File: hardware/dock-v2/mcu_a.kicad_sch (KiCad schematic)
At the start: 29 parts, among them SW301 SW_Push, SW302 SW_Push, U301 RP2354A, Y301 12MHz

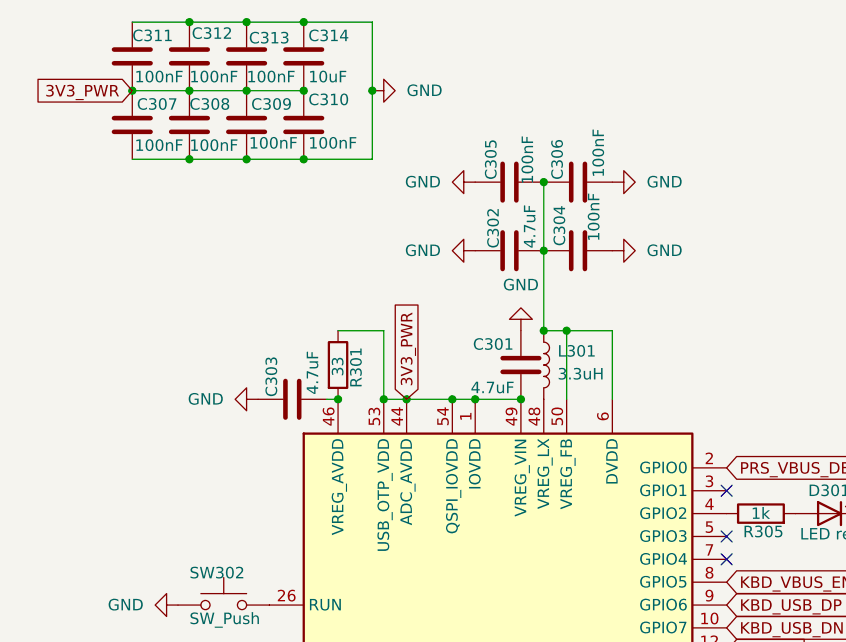
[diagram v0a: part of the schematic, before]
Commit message: Dock v2 schematic: PWR_FLAGs, one name per power net, ESP32 USB test pads dropped
- PWR_FLAGs on GND, VBUS_IN, 5V_PWR, A_1V1, A_VREG_AVDD, B_1V1, B_VREG_AVDD
  (each with a label at a pin of the net, which also names the five nets that
  were unnamed: VBUS_IN, A/B_1V1, A/B_VREG_AVDD)
- GNDPWR symbol -> GND; duplicate +3.3V/+5V power symbols and their now-dangling
  3V3_PWR/5V_PWR labels removed (connectivity verified identical before/after)
- TP501/TP502 (ESP32 GPIO18/19 USB pads) not needed: pins 26/27 are no-connects
  in the model; docs and guides updated (fallback flashing: TXD0/RXD0 pads)

ERC: 0 errors, 0 warnings. check_wiring.py: OK, wiring matches the guide.

Co-Authored-By: Claude Opus 5.5 <noreply@anthropic.com>
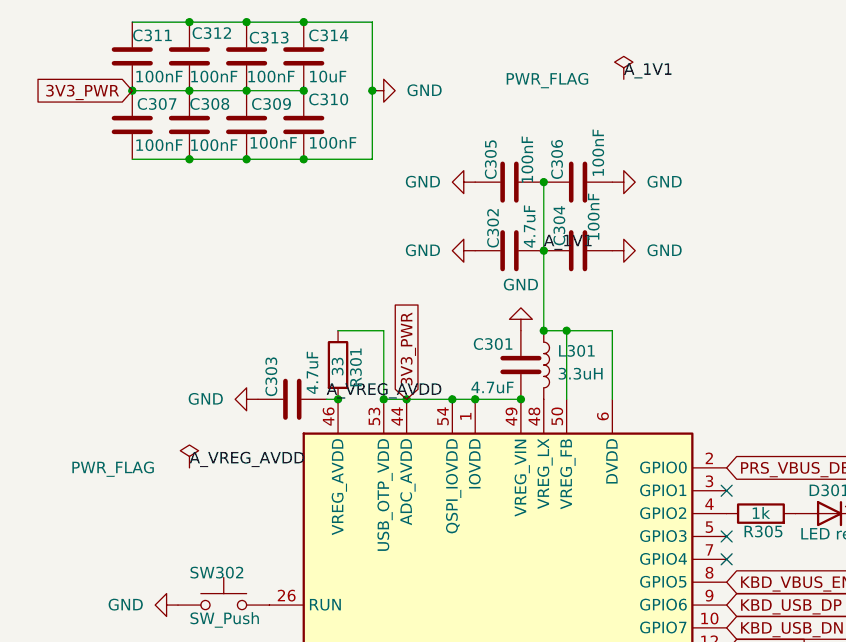
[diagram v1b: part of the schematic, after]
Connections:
- net A_1V1: now reaches C302.2, C304.1, C305.2, C306.1, L301.1, U301.23 (DVDD), U301.39 (DVDD), U301.50 (VREG_FB), U301.6 (DVDD)
- net A_VREG_AVDD: now reaches C303.2, R301.2, U301.46 (VREG_AVDD)
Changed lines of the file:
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@@
+		)
+	)
+	(label "A_1V1"
+		(at 189.23 57.15 0)
+		(fields_autoplaced yes)
+		(effects
+			(font
+				(size 1.27 1.27)
+			)
+			(justify left bottom)
+		)
+	)
+	(symbol
+		(lib_id "power:PWR_FLAG")
+		(at 198.12 38.1 0)
+		(unit 1)
+		(body_style 1)
+		(exclude_from_sim no)
+		(in_bom yes)
+		(on_board yes)
+		(in_pos_files yes)
+		(dnp no)
+		(fields_autoplaced yes)
+		(property "Reference" "#FLG0390"
+			(at 191.77 38.1 0)
+			(hide yes)
+			(show_name no)
+			(do_not_autoplace no)
+			(effects
+				(font
+					(size 1.27 1.27)
+				)
+			)
+		)
+		(property "Value" "PWR_FLAG"
+			(at 194.31 38.1 0)
+			(show_name no)
+			(do_not_autoplace no)
+			(effects
+				(font
+					(size 1.27 1.27)
+				)
+				(justify right)
+			)
+		)
+		(property "Footprint" ""
+			(at 198.12 38.1 0)
+			(hide yes)
+			(show_name no)
+			(do_not_autoplace no)
+			(effects
+				(font
+					(size 1.27 1.27)
+				)
+			)
+		)
+		(property "Datasheet" ""
+			(at 198.12 38.1 0)
+			(hide yes)
+			(show_name no)
+			(do_not_autoplace no)
+			(effects
+				(font
+					(size 1.27 1.27)
+				)
+			)
+		)
+		(property "Description" "Power symbol creates a global label with name \"GND\" , ground"
+			(at 198.12 38.1 0)
+			(hide yes)
+			(show_name no)
+			(do_not_autoplace no)
+			(effects
+				(font
+					(size 1.27 1.27)
+				)
+			)
+		)
+		(pin "1"
+		)
+		(instances
+			(project "dock-v2"
+				(path "/928a9dc6-b0ce-4f47-a17d-f26fd77e396a/bcfba91e-3181-4d07-9970-4b16b455c32a"
+					(reference "#FLG0390")
+					(unit 1)
+				)
+			)
+		)
+	)
+	(label "A_1V1"
+		(at 198.12 38.1 0)
+		(fields_autoplaced yes)
+		(effects
+			(font
+				(size 1.27 1.27)
+			)
+			(justify left bottom)
+		)
+	)
+	(label "A_VREG_AVDD"
+		(at 165.1 73.66 0)
+		(fields_autoplaced yes)
+		(effects
+			(font
+				(size 1.27 1.27)
+			)
+			(justify left bottom)
+		)
+	)
+	(symbol
+		(lib_id "power:PWR_FLAG")
+		(at 149.86 81.28 0)
+		(unit 1)
+		(body_style 1)
+		(exclude_from_sim no)
+		(in_bom yes)
+		(on_board yes)
+		(in_pos_files yes)
+		(dnp no)
+		(fields_autoplaced yes)
+		(property "Reference" "#FLG0391"
+			(at 143.51 81.28 0)
+			(hide yes)
+			(show_name no)
+			(do_not_autoplace no)
+			(effects
+				(font
+					(size 1.27 1.27)
+				)
+			)
+		)
+		(property "Value" "PWR_FLAG"
+			(at 146.05 81.28 0)
+			(show_name no)
+			(do_not_autoplace no)
+			(effects
+				(font
+					(size 1.27 1.27)
+				)
+				(justify right)
+			)
+		)
+		(property "Footprint" ""
+			(at 149.86 81.28 0)
+			(hide yes)
+			(show_name no)
+			(do_not_autoplace no)
+			(effects
+				(font
+					(size 1.27 1.27)
+				)
+			)
+		)
+		(property "Datasheet" ""
+			(at 149.86 81.28 0)
+			(hide yes)
+			(show_name no)
+			(do_not_autoplace no)
+			(effects
+				(font
+					(size 1.27 1.27)
+				)
+			)
+		)
+		(property "Description" "Power symbol creates a global label with name \"GND\" , ground"
+			(at 149.86 81.28 0)
+			(hide yes)
+			(show_name no)
+			(do_not_autoplace no)
+			(effects
+				(font
+					(size 1.27 1.27)
+				)
+			)
+		)
+		(pin "1"
+		)
+		(instances
+			(project "dock-v2"
+				(path "/928a9dc6-b0ce-4f47-a17d-f26fd77e396a/bcfba91e-3181-4d07-9970-4b16b455c32a"
+					(reference "#FLG0391")
+					(unit 1)
+				)
+			)
+		)
+	)
+	(label "A_VREG_AVDD"
+		(at 149.86 81.28 0)
+		(fields_autoplaced yes)
+		(effects
+			(font
+				(size 1.27 1.27)
+			)
+			(justify left bottom)
 		)
 	)
